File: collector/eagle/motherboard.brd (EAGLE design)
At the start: 85.1 x 56.8 mm, 9 parts

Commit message: Updated scheme of collector motherboard
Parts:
- moved U$3 70.3 mm to (75.8, 29.3), turned to 90 degrees
- moved R1 68.2 mm to (71.9, 39.5), turned to 180 degrees
- moved R2 60.2 mm to (71.9, 19.2), turned to 180 degrees
- moved U$1 52.6 mm to (16.0, 28.1), flipped to the bottom
- moved RGB_LED 29.4 mm to (28.7, 25.5), turned to 0 degrees
- moved R3 21.6 mm to (23.6, 16.6), turned to 0 degrees
- moved R5 18.1 mm to (30.0, 14.1), turned to 0 degrees
- moved R4 16.3 mm to (30.0, 19.2), turned to 0 degrees
- moved U$2 16.2 mm to (50.3, 26.8), flipped to the bottom
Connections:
- net GND: now also U$3.LED_GREEN_-, U$3.LED_YELLOW_-
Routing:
- net 3V3: track 108.3 -> 203.6 mm
- net PB9: track 59.8 -> 21.5 mm
- net GND: track 210.9 -> 239.9 mm
- net PC14: track 38.4 -> 12.3 mm
- net PC15: track 31.4 -> 5.67 mm
- net PC13: track 41.1 -> 16.7 mm
- net N$16: track 20.3 -> 2.39 mm
- net PA10: track 23.3 -> 7.24 mm
- net PA9: track 22.3 -> 9.77 mm
- net N$18: track 12.1 -> 2.39 mm
- net N$17: track 16.2 -> 8.74 mm
- net N$5: track 47.1 -> 50.3 mm
- net N$9: track 6.17 -> 8.33 mm
- net PB8: track 42.1 -> 43.2 mm
- net N$4: track 41.4 -> 42.4 mm
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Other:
- board size 85.1 x 56.8 mm -> 160 x 100 mm

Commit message: Tiny fixes on colletor's motherboard
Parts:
- moved RGB_LED 12.8 mm to (41.4, 27.1)
- moved R4 7.87 mm to (37.8, 19.2), turned to 180 degrees
- moved R5 7.87 mm to (37.8, 14.1), turned to 180 degrees
- moved R3 6.13 mm to (29.6, 18.0), turned to 270 degrees
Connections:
- net 3V3: now also RGB_LED.4
- net GND: no longer RGB_LED.4
- net PC13: now also RGB_LED.3; no longer RGB_LED.1
- net PC15: now also RGB_LED.1; no longer RGB_LED.3
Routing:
- net GND: track 239.9 -> 209.6 mm
- net 3V3: track 203.6 -> 229.8 mm
- net PC14: track 12.3 -> 19.2 mm
- net N$17: track 8.74 -> 4.19 mm
- net PC13: track 16.7 -> 13.1 mm
- net PC15: track 5.67 -> 7.47 mm
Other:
- board size 160 x 100 mm -> 82.8 x 54.1 mm
- board text added: "Гладцин А. М. <amgladtsin@mephi.ru>, Окунев Д. Ю. <dyokunev@mephi.ru> 0x8E30679C; Москва, ОЮТ УИ, МИФИ, 2016"
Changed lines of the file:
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@@
 <board>
 <plain>
-<wire x1="0" y1="0" x2="160" y2="0" width="0" layer="20"/>
-<wire x1="160" y1="0" x2="160" y2="100" width="0" layer="20"/>
-<wire x1="160" y1="100" x2="0" y2="100" width="0" layer="20"/>
-<wire x1="0" y1="100" x2="0" y2="0" width="0" layer="20"/>
+<wire x1="0" y1="0" x2="82.784" y2="0" width="0" layer="20"/>
+<wire x1="82.784" y1="0" x2="82.784" y2="54.026" width="0" layer="20"/>
+<wire x1="82.784" y1="54.026" x2="0" y2="54.026" width="0" layer="20"/>
+<wire x1="0" y1="54.026" x2="0" y2="0" width="0" layer="20"/>
+<text x="1.651" y="47.371" size="1.4224" layer="1" rot="R270">Гладцин А. М. &lt;amgladtsin@mephi.ru&gt;,
+Окунев Д. Ю. &lt;dyokunev@mephi.ru&gt; 0x8E30679C;
+Москва, ОЮТ УИ, МИФИ, 2016</text>
+<wire x1="0" y1="54.102" x2="82.804" y2="0" width="0.0508" layer="20"/>
+<wire x1="82.804" y1="53.975" x2="0" y2="0" width="0.0508" layer="20"/>
 </plain>
 <attributes>
@@
 <element name="R1" library="resistor" package="R1206" value="" x="71.882" y="39.497" rot="R180"/>
 <element name="R2" library="resistor" package="R1206" value="" x="71.882" y="19.177" rot="R180"/>
-<element name="R3" library="resistor" package="R1206" value="" x="23.622" y="16.637"/>
-<element name="R4" library="resistor" package="R1206" value="" x="29.972" y="19.177"/>
-<element name="R5" library="resistor" package="R1206" value="" x="29.972" y="14.097"/>
-<element name="RGB_LED" library="pinhead" package="2X02" value="" x="28.702" y="25.527"/>
+<element name="R3" library="resistor" package="R1206" value="" x="29.591" y="18.034" rot="R270"/>
+<element name="R4" library="resistor" package="R1206" value="" x="37.846" y="19.177" rot="R180"/>
+<element name="R5" library="resistor" package="R1206" value="" x="37.846" y="14.097" rot="R180"/>
+<element name="RGB_LED" library="pinhead" package="2X02" value="" x="41.402" y="27.051"/>
 <element name="U$1" library="ut-boards" package="HANRUN_HR911105A_15/10" value="HANRUN_HR911105A_15/10" x="16.002" y="28.067" rot="MR0"/>
 <element name="U$2" library="ut-boards" package="STM32F103C8T6_BOARD_BLACK" value="STM32F103C8T6_BOARD_BLACK" x="50.292" y="26.797" rot="MR0"/>
@@
 <contactref element="U$2" pad="GND@6"/>
 <contactref element="U$2" pad="GND@7"/>
-<contactref element="RGB_LED" pad="4"/>
 <contactref element="U$1" pad="GND@0"/>
 <contactref element="U$1" pad="GND@1"/>
@@
 <wire x1="12.192" y1="3.937" x2="19.812" y2="3.937" width="0.4064" layer="1"/>
 <wire x1="19.812" y1="3.937" x2="22.352" y2="6.477" width="0.4064" layer="1"/>
-<wire x1="29.972" y1="26.797" x2="31.242" y2="26.797" width="0.4064" layer="1"/>
-<wire x1="31.242" y1="26.797" x2="32.512" y2="28.067" width="0.4064" layer="1"/>
-<wire x1="32.512" y1="28.067" x2="36.322" y2="28.067" width="0.4064" layer="1"/>
-<wire x1="36.322" y1="28.067" x2="52.832" y2="44.577" width="0.4064" layer="1"/>
 <wire x1="60.452" y1="44.577" x2="64.389" y2="44.577" width="0.4064" layer="1"/>
 <wire x1="64.389" y1="44.577" x2="65.659" y2="43.307" width="0.4064" layer="1"/>
@@
 <wire x1="68.58" y1="2.667" x2="37.719" y2="2.667" width="0.4064" layer="1"/>
 <wire x1="37.719" y1="2.667" x2="36.449" y2="3.937" width="0.4064" layer="1"/>
-<wire x1="36.449" y1="3.937" x2="36.449" y2="3.937" width="0" layer="19" extent="1-16"/>
+<contactref element="RGB_LED" pad="4"/>
+<wire x1="36.322" y1="10.287" x2="41.275" y2="10.287" width="0.4064" layer="1"/>
+<wire x1="41.275" y1="10.287" x2="45.593" y2="14.605" width="0.4064" layer="1"/>
+<wire x1="45.593" y1="14.605" x2="45.593" y2="25.908" width="0.4064" layer="1"/>
+<wire x1="45.593" y1="25.908" x2="42.672" y2="28.321" width="0.4064" layer="1"/>
+<wire x1="36.322" y1="3.937" x2="36.449" y2="3.937" width="0" layer="19" extent="1-1"/>
 </signal>
 <signal name="PB8">
@@
 </signal>
 <signal name="PC13">
-<contactref element="RGB_LED" pad="1"/>
 <contactref element="R5" pad="1"/>
-<wire x1="28.55" y1="14.097" x2="23.622" y2="14.097" width="0.4064" layer="1"/>
-<wire x1="23.622" y1="14.097" x2="23.622" y2="19.177" width="0.4064" layer="1"/>
-<wire x1="23.622" y1="19.177" x2="27.432" y2="22.987" width="0.4064" layer="1"/>
-<wire x1="27.432" y1="22.987" x2="27.432" y2="24.257" width="0.4064" layer="1"/>
+<contactref element="RGB_LED" pad="3"/>
+<wire x1="39.268" y1="14.097" x2="42.672" y2="17.501" width="0.4064" layer="1"/>
+<wire x1="42.672" y1="17.501" x2="42.672" y2="25.781" width="0.4064" layer="1"/>
 </signal>
 <signal name="PC14">
 <contactref element="RGB_LED" pad="2"/>
 <contactref element="R3" pad="1"/>
-<wire x1="22.2" y1="16.637" x2="22.2" y2="21.565" width="0.4064" layer="1"/>
-<wire x1="22.2" y1="21.565" x2="27.432" y2="26.797" width="0.4064" layer="1"/>
-</signal>
-<signal name="PC15">
-<contactref element="RGB_LED" pad="3"/>
-<contactref element="R4" pad="1"/>
-<wire x1="28.55" y1="19.177" x2="29.972" y2="20.599" width="0.4064" layer="1"/>
-<wire x1="29.972" y1="20.599" x2="29.972" y2="24.257" width="0.4064" layer="1"/>
+<wire x1="29.591" y1="19.456" x2="29.591" y2="28.067" width="0.4064" layer="1"/>
+<wire x1="29.591" y1="28.067" x2="38.989" y2="28.067" width="0.4064" layer="1"/>
+<wire x1="38.989" y1="28.067" x2="40.132" y2="28.321" width="0.4064" layer="1"/>
 </signal>
 <signal name="N$16">
 <contactref element="R4" pad="2"/>
 <contactref element="U$2" pad="PC15"/>
-<wire x1="33.782" y1="19.177" x2="31.394" y2="19.177" width="0.4064" layer="1"/>
+<wire x1="36.424" y1="19.177" x2="33.782" y2="19.177" width="0.4064" layer="1"/>
 </signal>
 <signal name="N$17">
 <contactref element="R3" pad="2"/>
 <contactref element="U$2" pad="PC14"/>
-<wire x1="33.782" y1="16.637" x2="25.044" y2="16.637" width="0.4064" layer="1"/>
+<wire x1="33.782" y1="16.637" x2="29.591" y2="16.612" width="0.4064" layer="1"/>
 </signal>
 <signal name="N$18">
 <contactref element="R5" pad="2"/>
 <contactref element="U$2" pad="PC13"/>
-<wire x1="33.782" y1="14.097" x2="31.394" y2="14.097" width="0.4064" layer="1"/>
+<wire x1="33.782" y1="14.097" x2="36.424" y2="14.097" width="0.4064" layer="1"/>
+</signal>
+<signal name="PC15">
+<contactref element="R4" pad="1"/>
+<contactref element="RGB_LED" pad="1"/>
+<wire x1="39.268" y1="19.177" x2="40.132" y2="19.177" width="0.4064" layer="1"/>
+<wire x1="40.132" y1="19.177" x2="40.132" y2="25.781" width="0.4064" layer="1"/>
 </signal>
 </signals>
 </board>
 </drawing>
+<compatibility>
+<note version="6.3" minversion="6.2.2" severity="warning">
+Since Version 6.2.2 text objects can contain more than one line,
+which will not be processed correctly with this version.
+</note>
+</compatibility>
 </eagle>

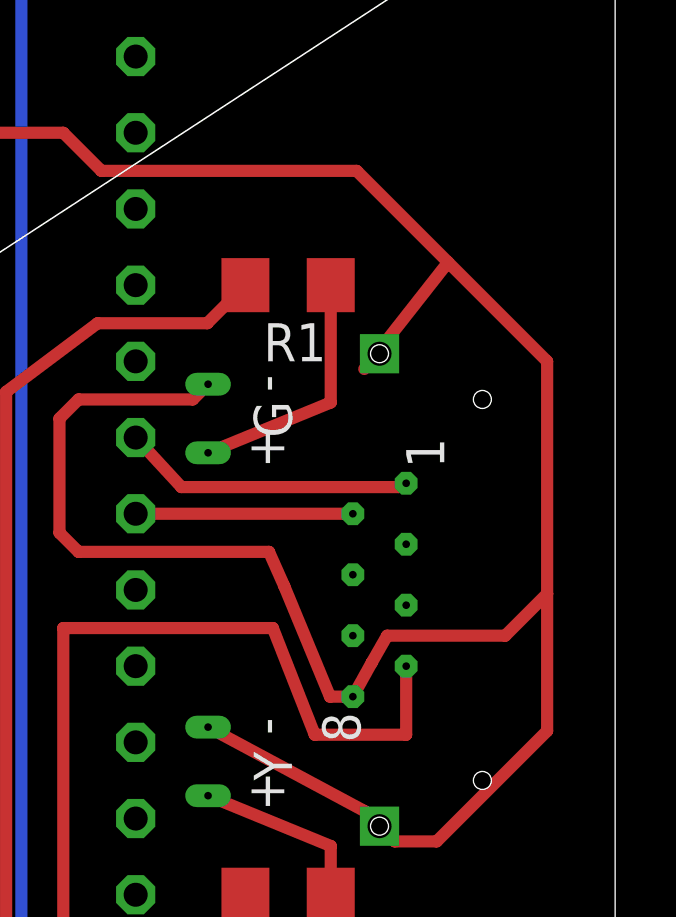
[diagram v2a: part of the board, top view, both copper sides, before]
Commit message: Added a pull-up resistor for UART-RX of collector
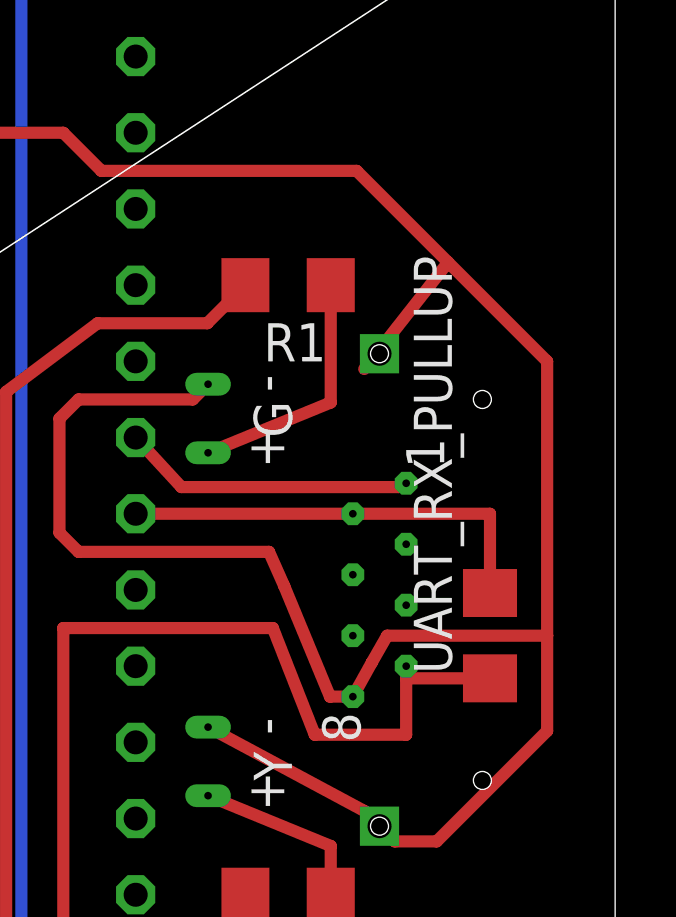
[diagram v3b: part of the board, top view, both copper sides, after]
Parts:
- added UART_RX_PULLUP: ~2K, resistor:R1206
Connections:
- net PA9 renamed PA9_(UART_TX)
- removed net PA10: U$2.PA10, U$3.P2
- new net PA10_(UART_RX): U$2.PA10, U$3.P2, UART_RX_PULLUP.2
- net 3V3: now also UART_RX_PULLUP.1
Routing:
- net PA10_(UART_RX): track 0.00 -> 14.5 mm
- net PA10: track 7.24 -> 0.00 mm
- net 3V3: track 229.8 -> 233.0 mm
- net GND: track 209.6 -> 209.0 mm
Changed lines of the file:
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@@
 <element name="U$2" library="ut-boards" package="STM32F103C8T6_BOARD_BLACK" value="STM32F103C8T6_BOARD_BLACK" x="50.292" y="26.797" rot="MR0"/>
 <element name="U$3" library="ut-connectors" package="RJHSE-5481_(RJ45)" value="RJHSE-5481_(RJ45)" x="75.819" y="29.337" rot="R90"/>
+<element name="UART_RX_PULLUP" library="resistor" package="R1206" value="~2K" x="78.613" y="27.813" rot="R90"/>
 </elements>
 <signals>
@@
 <wire x1="74.168" y1="43.307" x2="77.216" y2="40.259" width="0.4064" layer="1"/>
 <wire x1="77.216" y1="40.259" x2="80.518" y2="36.957" width="0.4064" layer="1"/>
-<wire x1="80.518" y1="36.957" x2="80.518" y2="29.21" width="0.4064" layer="1"/>
-<wire x1="80.518" y1="29.21" x2="79.121" y2="27.813" width="0.4064" layer="1"/>
-<wire x1="79.121" y1="27.813" x2="75.184" y2="27.813" width="0.4064" layer="1"/>
+<wire x1="80.518" y1="36.957" x2="80.518" y2="27.813" width="0.4064" layer="1"/>
+<wire x1="80.518" y1="27.813" x2="75.184" y2="27.813" width="0.4064" layer="1"/>
 <wire x1="75.184" y1="27.813" x2="74.676" y2="26.924" width="0.4064" layer="1"/>
 <wire x1="74.676" y1="26.924" x2="74.041" y2="25.781" width="0.4064" layer="1"/>
 <wire x1="77.216" y1="40.259" x2="74.422" y2="36.703" width="0.4064" layer="1"/>
-<wire x1="80.518" y1="29.21" x2="80.518" y2="24.638" width="0.4064" layer="1"/>
+<wire x1="80.518" y1="27.813" x2="80.518" y2="24.638" width="0.4064" layer="1"/>
 <wire x1="80.518" y1="24.638" x2="76.835" y2="20.955" width="0.4064" layer="1"/>
 <wire x1="76.835" y1="20.955" x2="75.438" y2="20.955" width="0.4064" layer="1"/>
@@
 <wire x1="45.593" y1="14.605" x2="45.593" y2="25.908" width="0.4064" layer="1"/>
 <wire x1="45.593" y1="25.908" x2="42.672" y2="28.321" width="0.4064" layer="1"/>
+<contactref element="UART_RX_PULLUP" pad="1"/>
+<wire x1="78.613" y1="26.391" x2="75.819" y2="26.391" width="0.4064" layer="1"/>
+<wire x1="75.819" y1="26.391" x2="75.819" y2="26.797" width="0.4064" layer="1"/>
 <wire x1="36.322" y1="3.937" x2="36.449" y2="3.937" width="0" layer="19" extent="1-1"/>
 </signal>
@@
 <wire x1="73.304" y1="20.803" x2="69.215" y2="22.479" width="0.4064" layer="1"/>
 </signal>
-<signal name="PA9">
+<signal name="PA9_(UART_TX)">
 <contactref element="U$2" pad="PA9"/>
 <contactref element="U$3" pad="P1"/>
@@
 <wire x1="75.565" y1="32.766" x2="75.819" y2="32.893" width="0.4064" layer="1"/>
 </signal>
-<signal name="PA10">
+<signal name="PA10_(UART_RX)">
 <contactref element="U$2" pad="PA10"/>
 <contactref element="U$3" pad="P2"/>
 <wire x1="66.802" y1="31.877" x2="74.041" y2="31.877" width="0.4064" layer="1"/>
+<contactref element="UART_RX_PULLUP" pad="2"/>
+<wire x1="78.613" y1="29.235" x2="78.613" y2="31.877" width="0.4064" layer="1"/>
+<wire x1="78.613" y1="31.877" x2="74.041" y2="31.877" width="0.4064" layer="1"/>
 </signal>
 <signal name="PC13">
